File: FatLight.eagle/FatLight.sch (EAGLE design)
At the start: 25 parts, among them J1 12V, Q1 IRF540, Q2 IRF540, Q3 IRF540, Q4 16MHz, U1 ATMEGA328P-PU

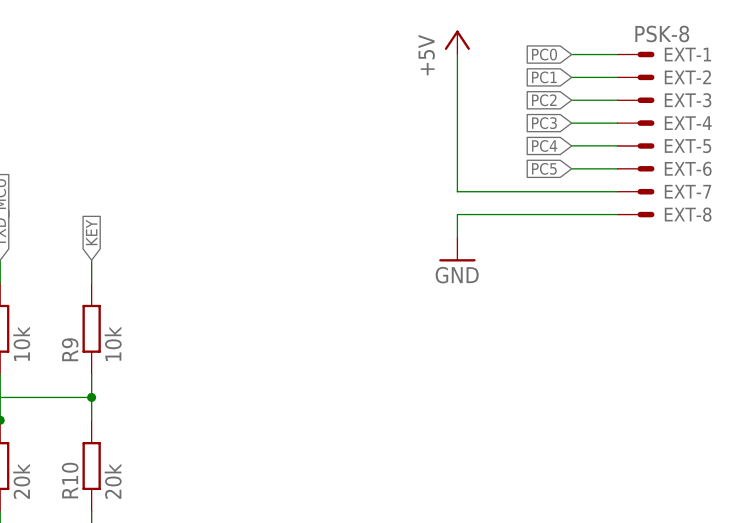
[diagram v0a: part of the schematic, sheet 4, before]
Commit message: Vias und Restringe vergrößert, richtige Widerstandsgrößen verwendet, Platinengröße angepasst, Kondensator für Ext-Konnektor eingefügt.
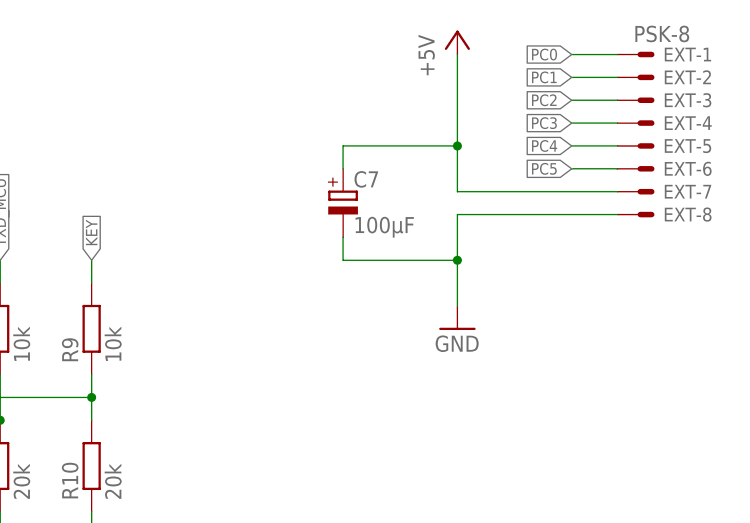
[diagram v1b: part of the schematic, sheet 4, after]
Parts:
- added C7: 100µF, rcl:CPOL-EUE2.5-5
- R1, R10, R2, R3, R4, R7, R8, R9: device rcl:R-EU_0204/5 -> rcl:R-EU_0207/7
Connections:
- net +5V: now also C7.+
- net GND: now also C7.-
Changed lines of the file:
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@@
 <part name="C3" library="rcl" deviceset="C-EU" device="025-025X050" value="22pF"/>
 <part name="C4" library="rcl" deviceset="C-EU" device="025-025X050" value="22pF"/>
-<part name="R1" library="rcl" deviceset="R-EU_" device="0204/5" value="10k"/>
-<part name="R2" library="rcl" deviceset="R-EU_" device="0204/5" value="100k"/>
-<part name="R3" library="rcl" deviceset="R-EU_" device="0204/5" value="100k"/>
-<part name="R4" library="rcl" deviceset="R-EU_" device="0204/5" value="100k"/>
+<part name="R1" library="rcl" deviceset="R-EU_" device="0207/7" value="10k"/>
+<part name="R2" library="rcl" deviceset="R-EU_" device="0207/7" value="100k"/>
+<part name="R3" library="rcl" deviceset="R-EU_" device="0207/7" value="100k"/>
+<part name="R4" library="rcl" deviceset="R-EU_" device="0207/7" value="100k"/>
 <part name="GND1" library="supply1" deviceset="GND" device=""/>
 <part name="GND2" library="supply1" deviceset="GND" device=""/>
@@
 <part name="P+8" library="supply1" deviceset="+5V" device=""/>
 <part name="GND11" library="supply1" deviceset="GND" device=""/>
-<part name="R7" library="rcl" deviceset="R-EU_" device="0204/5" value="10k"/>
-<part name="R8" library="rcl" deviceset="R-EU_" device="0204/5" value="20k"/>
-<part name="R9" library="rcl" deviceset="R-EU_" device="0204/5" value="10k"/>
-<part name="R10" library="rcl" deviceset="R-EU_" device="0204/5" value="20k"/>
+<part name="R7" library="rcl" deviceset="R-EU_" device="0207/7" value="10k"/>
+<part name="R8" library="rcl" deviceset="R-EU_" device="0207/7" value="20k"/>
+<part name="R9" library="rcl" deviceset="R-EU_" device="0207/7" value="10k"/>
+<part name="R10" library="rcl" deviceset="R-EU_" device="0207/7" value="20k"/>
 <part name="EXT" library="con-molex" deviceset="22-23-2081" device="" value="PSK-8"/>
 <part name="P+9" library="supply1" deviceset="+5V" device=""/>
 <part name="GND12" library="supply1" deviceset="GND" device=""/>
+<part name="C7" library="rcl" deviceset="CPOL-EU" device="E2.5-5" value="100µF"/>
 </parts>
 <sheets>
@@
 <instance part="EXT" gate="-8" x="149.86" y="119.38"/>
 <instance part="P+9" gate="1" x="129.54" y="139.7"/>
-<instance part="GND12" gate="1" x="129.54" y="114.3"/>
+<instance part="GND12" gate="1" x="129.54" y="106.68"/>
+<instance part="C7" gate="G$1" x="116.84" y="121.92"/>
 </instances>
 <busses>
@@
 <segment>
 <pinref part="P+9" gate="1" pin="+5V"/>
-<wire x1="129.54" y1="137.16" x2="129.54" y2="121.92" width="0.1524" layer="91"/>
+<wire x1="129.54" y1="137.16" x2="129.54" y2="127" width="0.1524" layer="91"/>
 <pinref part="EXT" gate="-7" pin="S"/>
+<wire x1="129.54" y1="127" x2="129.54" y2="121.92" width="0.1524" layer="91"/>
 <wire x1="129.54" y1="121.92" x2="147.32" y2="121.92" width="0.1524" layer="91"/>
+<pinref part="C7" gate="G$1" pin="+"/>
+<wire x1="116.84" y1="124.46" x2="116.84" y2="127" width="0.1524" layer="91"/>
+<wire x1="116.84" y1="127" x2="129.54" y2="127" width="0.1524" layer="91"/>
+<junction x="129.54" y="127"/>
 </segment>
 </net>
@@
 <pinref part="GND12" gate="1" pin="GND"/>
 <pinref part="EXT" gate="-8" pin="S"/>
-<wire x1="129.54" y1="116.84" x2="129.54" y2="119.38" width="0.1524" layer="91"/>
+<wire x1="129.54" y1="109.22" x2="129.54" y2="114.3" width="0.1524" layer="91"/>
+<wire x1="129.54" y1="114.3" x2="129.54" y2="119.38" width="0.1524" layer="91"/>
 <wire x1="129.54" y1="119.38" x2="147.32" y2="119.38" width="0.1524" layer="91"/>
-</segment>
-</net>
+<pinref part="C7" gate="G$1" pin="-"/>
+<wire x1="116.84" y1="116.84" x2="116.84" y2="114.3" width="0.1524" layer="91"/>
+<wire x1="116.84" y1="114.3" x2="129.54" y2="114.3" width="0.1524" layer="91"/>
+<junction x="129.54" y="114.3"/>
+</segment>
+</net>

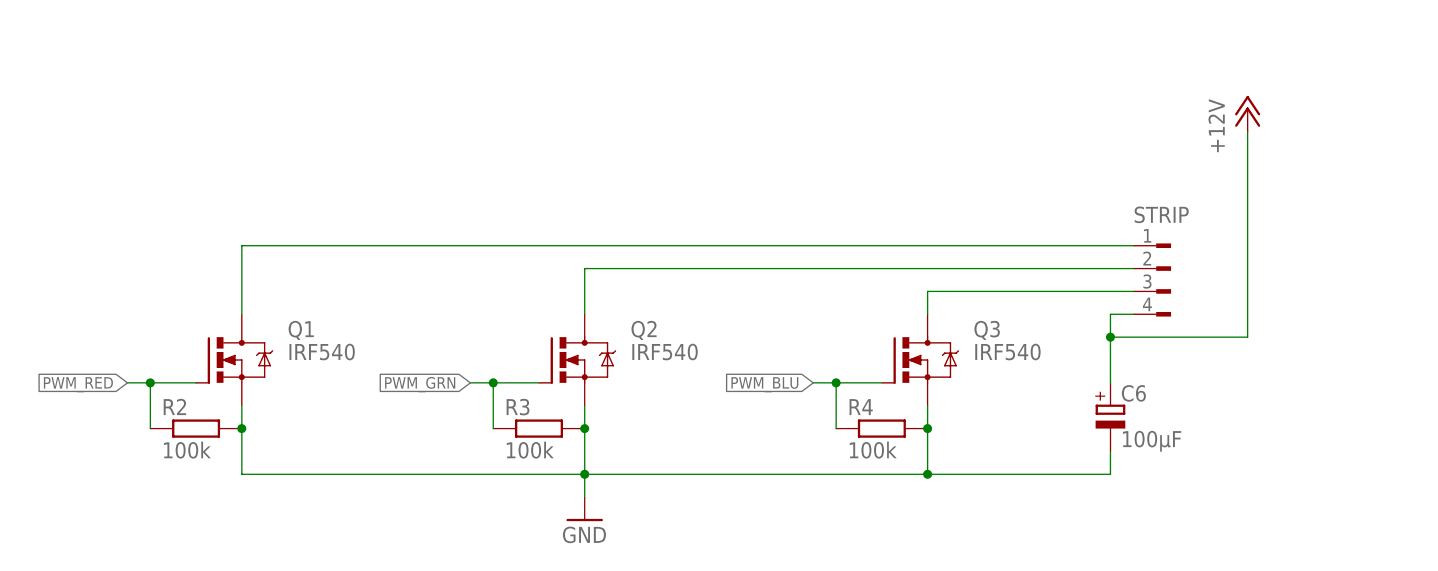
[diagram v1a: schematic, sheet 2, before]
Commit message: Optimierung des Boards
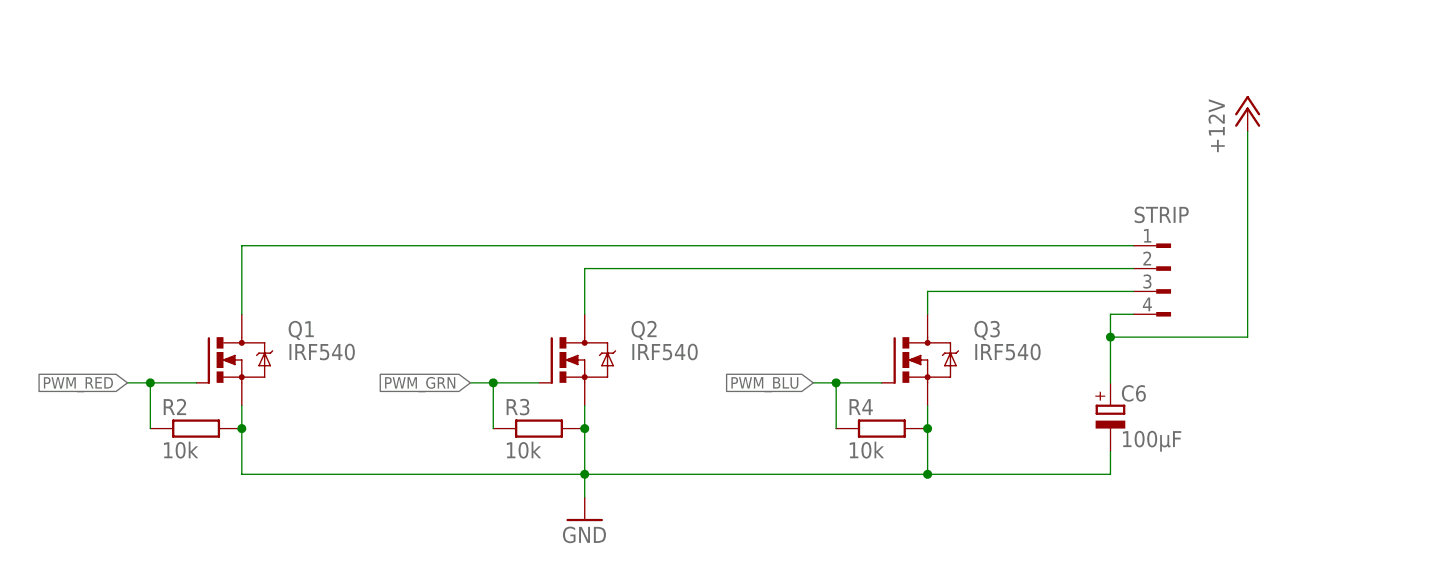
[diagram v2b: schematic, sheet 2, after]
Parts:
- R2, R3, R4: value 100k -> 10k
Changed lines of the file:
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@@
 <part name="C4" library="rcl" deviceset="C-EU" device="025-025X050" value="22pF"/>
 <part name="R1" library="rcl" deviceset="R-EU_" device="0207/7" value="10k"/>
-<part name="R2" library="rcl" deviceset="R-EU_" device="0207/7" value="100k"/>
-<part name="R3" library="rcl" deviceset="R-EU_" device="0207/7" value="100k"/>
-<part name="R4" library="rcl" deviceset="R-EU_" device="0207/7" value="100k"/>
+<part name="R2" library="rcl" deviceset="R-EU_" device="0207/7" value="10k"/>
+<part name="R3" library="rcl" deviceset="R-EU_" device="0207/7" value="10k"/>
+<part name="R4" library="rcl" deviceset="R-EU_" device="0207/7" value="10k"/>
 <part name="GND1" library="supply1" deviceset="GND" device=""/>
 <part name="GND2" library="supply1" deviceset="GND" device=""/>
